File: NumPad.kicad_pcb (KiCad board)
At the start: 2 copper layers, 60.7 x 98.9 mm, 112 parts, among them J1 Micro_SD_Card_Det, J2 OLED1, J3 OLED2, J4 Conn_01x05_Female, SW1 SW_SPST, SW10 SW_SPST, SW11 SW_SPST, SW12 SW_SPST, SW13 SW_SPST, SW14 SW_SPST, SW15 SW_SPST, SW16 SW_SPST, SW17 SW_SPST, SW18 SW_SPST, SW19 SW_SPST, SW2 SW_SPST, SW20 SW_SPST, SW21 SW_SPST, SW22 SW_SPST, SW23 SW_SPST, SW24 SW_SPST, SW25 SW_BUTTONRESET, SW26 SW_BUTTON2, SW27 SW_BUTTON1, SW28 SW_BOOT0, SW29 Rotary_Encoder_Switch, SW3 SW_SPST, SW4 SW_SPST, SW5 SW_SPST, SW6 SW_SPST, SW7 SW_SPST, SW8 SW_SPST, SW9 SW_SPST, U1 LM117_TO3, U2 STM32F072C8Tx, U3 74AHCT1G08

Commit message: PCB Update
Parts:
- C1, C12, C13, C2, C3, C4, C5, C6, C7, C9, D10, D11, D12, D13, D14, D15, D16, D17, D18, D19, D2, D20, D21, D22, D23, D24, D25, D3, D4, D5, D6, D7, D8, D9, R1, R10, R2, R3, R6, R7, U1, U3: moved to B.Cu
- moved R10 159.1 mm to (71.5, 55.2)
- moved C6 148.5 mm to (27.7, 166.0)
- moved R9 141.5 mm to (94.6, 57.1)
- moved R8 136.8 mm to (95.3, 62.7)
- moved C3 135.1 mm to (46.7, 166.0)
- moved R5 126.2 mm to (119.4, 174.6)
- moved J4 123.0 mm to (104.8, 178.6), turned to 90 degrees
- moved U3 122.1 mm to (103.8, 69.9), turned to 270 degrees
- moved R7 121.4 mm to (103.8, 75.2)
- moved C2 109.0 mm to (116.8, 83.4)
- moved C1 108.7 mm to (116.8, 80.3)
- moved R4 102.1 mm to (127.7, 174.9)
- moved R1 98.8 mm to (130.8, 73.4)
- moved R3 96.9 mm to (151.3, 78.8)
- moved R2 93.3 mm to (124.1, 72.6)
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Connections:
- C1 pad 2: +5V -> GND
- C10 pad 2: +5V -> GND
- C11 pad 2: +5V -> GND
- C12 pad 2: +5V -> GND
- C13 pad 2: +5V -> GND
- C14 pad 2: +5V -> GND
- C2 pad 2: +5V -> GND
- C3 pad 2: +5V -> GND
- C4 pad 2: +5V -> GND
- C5 pad 2: +5V -> GND
- C6 pad 2: +5V -> GND
- C7 pad 2: +5V -> GND
- C8 pad 2: +5V -> GND
- C9 pad 2: +5V -> GND
- D1 pad 1: +5V -> GND
- D26 pad 2: Net-(D32-Pad2) -> Net-(D26-Pad2)
- D26 pad 3: +5V -> GND
- D26 pad 4: Net-(D26-Pad2) -> Net-(D26-Pad4)
- D27 pad 2: Net-(D32-Pad2) -> Net-(D27-Pad2)
- D27 pad 3: +5V -> GND
- D27 pad 4: Net-(D26-Pad2) -> Net-(D27-Pad4)
- D28 pad 2: Net-(D32-Pad2) -> Net-(D28-Pad2)
- D28 pad 3: +5V -> GND
- D28 pad 4: Net-(D26-Pad2) -> Net-(D28-Pad4)
- D29 pad 2: Net-(D32-Pad2) -> Net-(D29-Pad2)
- D29 pad 3: +5V -> GND
- D29 pad 4: Net-(D26-Pad2) -> Net-(D29-Pad4)
- D30 pad 2: Net-(D32-Pad2) -> Net-(D30-Pad2)
- D30 pad 3: +5V -> GND
- D30 pad 4: Net-(D26-Pad2) -> Net-(D30-Pad4)
- D31 pad 2: Net-(D32-Pad2) -> Net-(D31-Pad2)
- D31 pad 3: +5V -> GND
- D31 pad 4: Net-(D26-Pad2) -> Net-(D31-Pad4)
- D32 pad 3: +5V -> GND
- D33 pad 2: Net-(D32-Pad2) -> Net-(D33-Pad2)
- D33 pad 3: +5V -> GND
- D33 pad 4: Net-(D26-Pad2) -> Net-(D27-Pad2)
- D34 pad 2: Net-(D32-Pad2) -> Net-(D34-Pad2)
- D34 pad 3: +5V -> GND
- D34 pad 4: Net-(D26-Pad2) -> Net-(D28-Pad2)
- D35 pad 2: Net-(D32-Pad2) -> Net-(D35-Pad2)
- D35 pad 3: +5V -> GND
- D35 pad 4: Net-(D26-Pad2) -> Net-(D29-Pad2)
- D36 pad 2: Net-(D32-Pad2) -> Net-(D36-Pad2)
- D36 pad 3: +5V -> GND
- D36 pad 4: Net-(D26-Pad2) -> Net-(D30-Pad2)
- D37 pad 2: Net-(D32-Pad2) -> Net-(D37-Pad2)
- D37 pad 3: +5V -> GND
- D37 pad 4: Net-(D26-Pad2) -> Net-(D31-Pad2)
- D38 pad 2: Net-(D32-Pad2) -> Net-(D38-Pad2)
- D38 pad 3: +5V -> GND
- D38 pad 4: Net-(D26-Pad2) -> Net-(D32-Pad2)
- D39 pad 2: Net-(D32-Pad2) -> Net-(D39-Pad2)
- D39 pad 3: +5V -> GND
- D39 pad 4: Net-(D26-Pad2) -> Net-(D33-Pad2)
- D40 pad 2: Net-(D32-Pad2) -> Net-(D40-Pad2)
- D40 pad 3: +5V -> GND
- D40 pad 4: Net-(D26-Pad2) -> Net-(D34-Pad2)
- D41 pad 2: Net-(D32-Pad2) -> Net-(D41-Pad2)
- D41 pad 3: +5V -> GND
- D41 pad 4: Net-(D26-Pad2) -> Net-(D35-Pad2)
- D42 pad 2: Net-(D32-Pad2) -> Net-(D42-Pad2)
- D42 pad 3: +5V -> GND
- D42 pad 4: Net-(D26-Pad2) -> Net-(D36-Pad2)
- D43 pad 2: Net-(D32-Pad2) -> Net-(D43-Pad2)
- D43 pad 3: +5V -> GND
- D43 pad 4: Net-(D26-Pad2) -> Net-(D37-Pad2)
- D44 pad 2: Net-(D32-Pad2) -> Net-(D27-Pad4)
- D44 pad 3: +5V -> GND
- D44 pad 4: Net-(D26-Pad2) -> Net-(D38-Pad2)
- D45 pad 2: Net-(D32-Pad2) -> Net-(D28-Pad4)
- D45 pad 3: +5V -> GND
- D45 pad 4: Net-(D26-Pad2) -> Net-(D39-Pad2)
- D46 pad 2: Net-(D32-Pad2) -> Net-(D29-Pad4)
- D46 pad 3: +5V -> GND
- D46 pad 4: Net-(D26-Pad2) -> Net-(D40-Pad2)
- D47 pad 2: Net-(D32-Pad2) -> Net-(D30-Pad4)
- D47 pad 3: +5V -> GND
- D47 pad 4: Net-(D26-Pad2) -> Net-(D41-Pad2)
- D48 pad 2: Net-(D32-Pad2) -> Net-(D31-Pad4)
- D48 pad 3: +5V -> GND
- D48 pad 4: Net-(D26-Pad2) -> Net-(D42-Pad2)
- D49 pad 2: Net-(D32-Pad2) -> Net-(D49-Pad2)
- D49 pad 3: +5V -> GND
- D49 pad 4: Net-(D26-Pad2) -> Net-(D43-Pad2)
- J1 pad 11: +5V -> GND
- J1 pad 6: +5V -> GND
- J2 pad 3: +5V -> GND
- J3 pad 3: +5V -> GND
- J4 pad 4: +5V -> GND
- R1 pad 1: +5V -> GND
- R2 pad 1: +5V -> GND
- R6 pad 2: +5V -> GND
- R7 pad 1: +5V -> GND
- RV1 pad 1: +5V -> GND
- SW25 pad 1: +5V -> GND
- SW26 pad 2: +5V -> GND
- SW27 pad 2: +5V -> GND
- SW29 pad C: +5V -> GND
- SW29 pad S2: +5V -> GND
- U1 pad 1: +5V -> GND
- U2 pad 1: +5V -> GND
- U2 pad 23: +5V -> GND
- U2 pad 35: +5V -> GND
- U2 pad 47: +5V -> GND
- U2 pad 8: +5V -> GND
- U3 pad 3: +5V -> GND
- USB1 pad 1: +5V -> GND
- USB1 pad 12: +5V -> GND
- USB1 pad 13: +5V -> GND

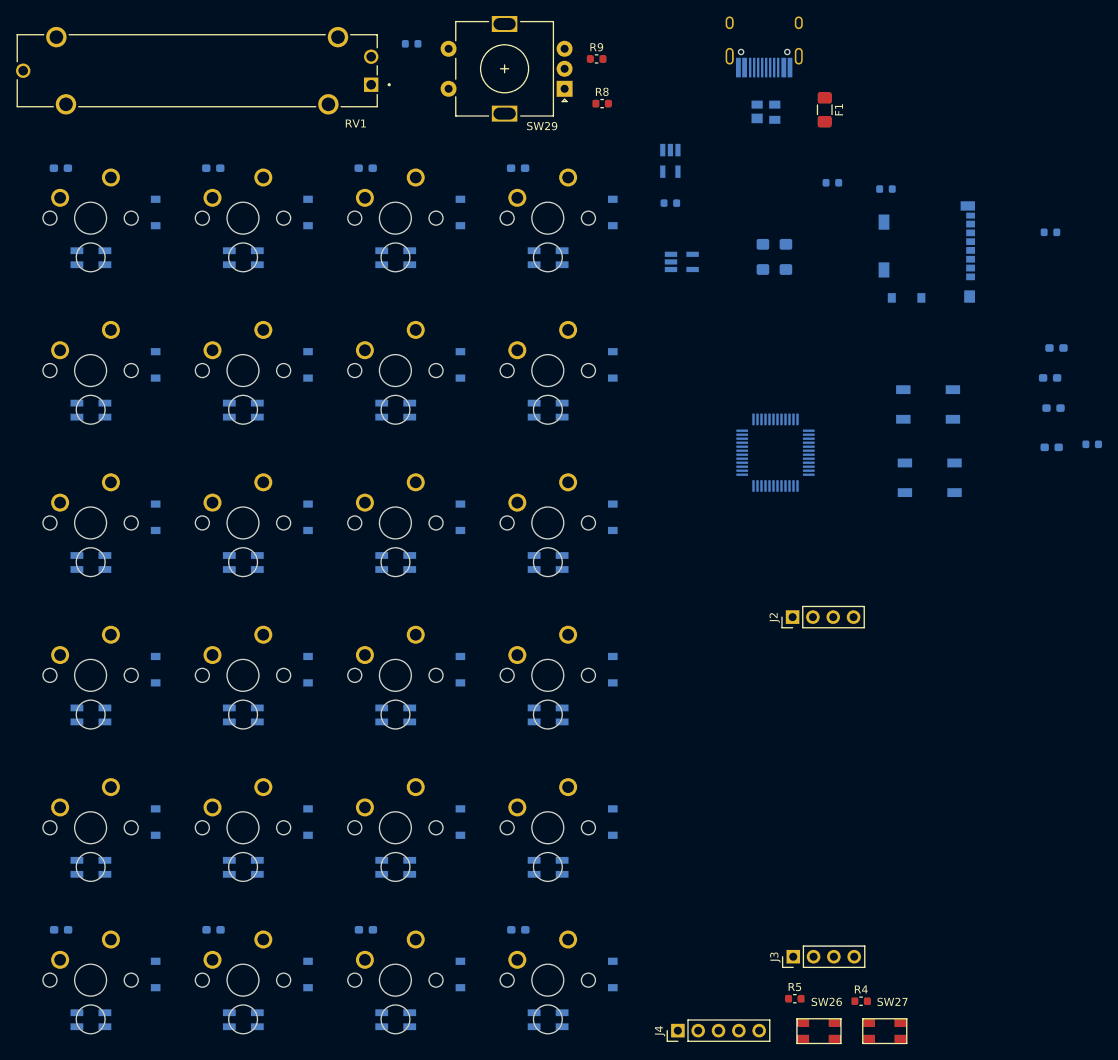
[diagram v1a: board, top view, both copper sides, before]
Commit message: Add footprints libs
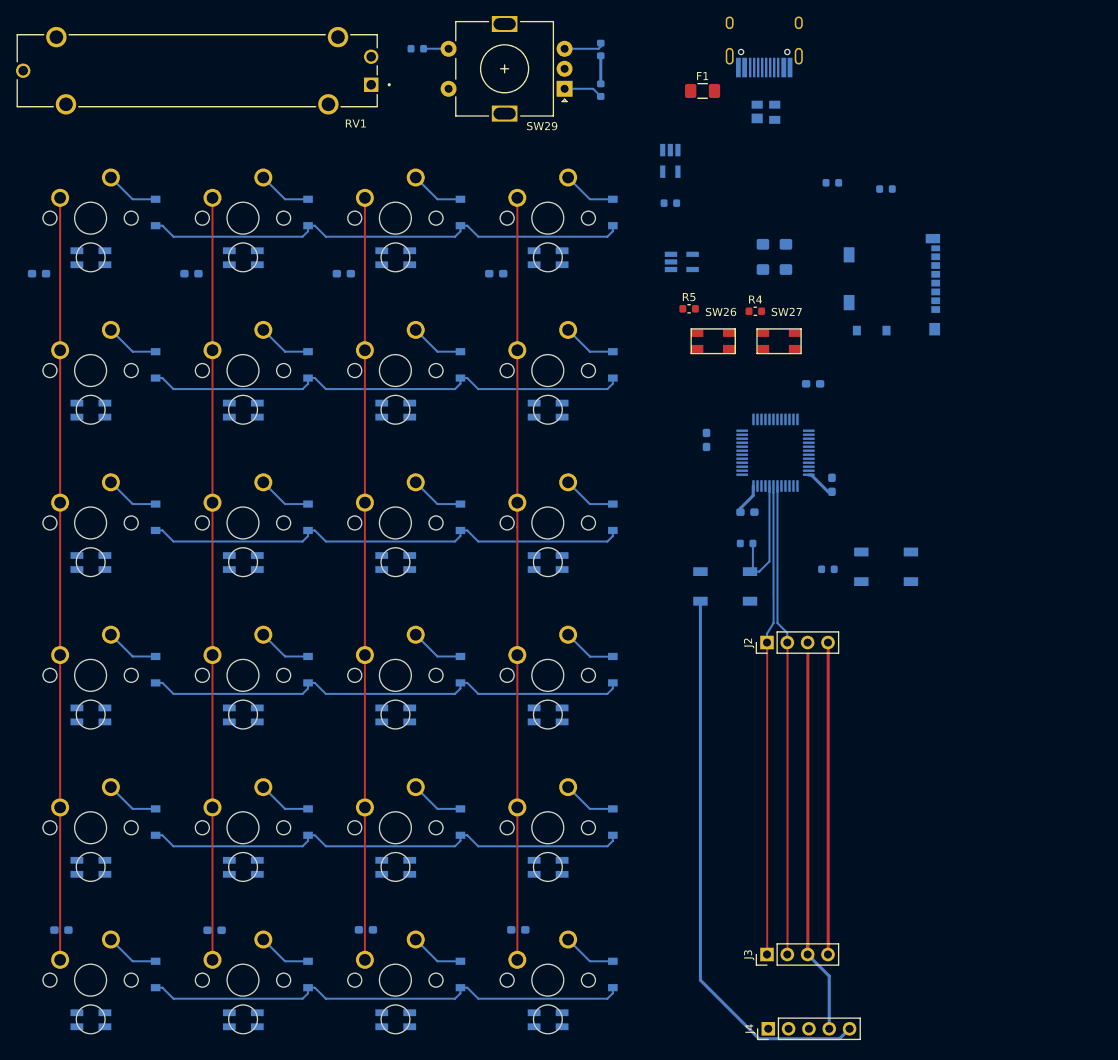
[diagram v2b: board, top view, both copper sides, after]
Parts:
- R8, R9: moved to B.Cu
- moved C12 140.1 mm to (27.7, 166.0), turned to 180 degrees
- moved C7 120.8 mm to (46.9, 166.0)
- moved C6 100.4 mm to (113.5, 113.8)
- moved SW26 87.2 mm to (110.2, 92.4)
- moved SW27 87.2 mm to (118.4, 92.4)
- moved R4 87.2 mm to (114.5, 88.7)
- moved R5 87.2 mm to (106.2, 88.4)
- moved C3 86.9 mm to (108.3, 104.8), turned to 270 degrees
- moved R3 50.5 mm to (123.5, 120.9)
- moved R6 44.9 mm to (113.4, 117.7), turned to 180 degrees
- moved SW28 34.1 mm to (110.7, 123.1)
- moved C4 30.7 mm to (121.7, 97.7), turned to 180 degrees
- moved C5 30.4 mm to (124.0, 110.4), turned to 90 degrees
- moved F1 15.5 mm to (107.9, 61.1), turned to 0 degrees
- moved C10 13.5 mm to (44.0, 84.0), turned to 180 degrees
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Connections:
- C10 pad 1: +3V3 -> +5V
- C11 pad 1: +3V3 -> +5V
- C12 pad 1: +3V3 -> +5V
- C13 pad 1: +3V3 -> +5V
- C14 pad 1: +3V3 -> +5V
- C7 pad 1: +3V3 -> +5V
- C8 pad 1: +3V3 -> +5V
- C9 pad 1: +3V3 -> +5V
- U2 pad 25: col3 -> POT_SLIDER
- U2 pad 26: row0 -> Net-(U2-Pad26)
- U2 pad 27: row1 -> Net-(U2-Pad27)
- U2 pad 28: row2 -> Net-(U2-Pad28)
- U2 pad 29: row3 -> Net-(U2-Pad29)
- U2 pad 3: Net-(U2-Pad3) -> col3
- U2 pad 4: Net-(U2-Pad4) -> row0
- U2 pad 40: POT_SLIDER -> Net-(U2-Pad40)
- U2 pad 45: Net-(U2-Pad45) -> row3
- U2 pad 5: Net-(U2-Pad5) -> row1
- U2 pad 6: Net-(U2-Pad6) -> row2
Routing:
- net col3: track 0.00 -> 95.2 mm
- net col2: track 0.00 -> 95.2 mm
- net col1: track 0.00 -> 95.2 mm
- net col0: track 0.00 -> 95.2 mm
- net +3V3: track 0.00 -> 80.8 mm
- net row4: track 0.00 -> 61.8 mm
- net row5: track 0.00 -> 61.8 mm
- net row2: track 0.00 -> 61.8 mm
- net row1: track 0.00 -> 61.8 mm
- net row0: track 0.00 -> 61.8 mm
- net row3: track 0.00 -> 61.8 mm
- net SCK: track 0.00 -> 59.1 mm
- net SDA: track 0.00 -> 58.0 mm
- net GND: track 0.00 -> 49.4 mm
- net +5V: track 0.00 -> 39.0 mm
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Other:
- net class Default: via_dia 0.8 -> 0.6
- net class power added: clearance 0.2, trace_width 0.38, via_dia 0.6, via_drill 0.4

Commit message: Update PCB
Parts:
- D26, D27, D28, D29, D30, D31, D32, D33, D34, D35, D36, D37, D38, D39, D40, D41, D42, D43, D44, D45, D46, D47, D48, D49: footprint LED_SMD:LED_SK6812MINI_PLCC4_3.5x3.5mm_P1.75mm -> keyboard_parts:YS-SK6812MINI-E
- moved C4 1.19 mm to (121.7, 96.5)
- turned D26 to 0 degrees
- turned D27 to 0 degrees
- turned D28 to 0 degrees
- turned D29 to 0 degrees
- turned D30 to 0 degrees
- turned D31 to 0 degrees
- turned D32 to 0 degrees
- turned D33 to 0 degrees
- turned D34 to 0 degrees
- turned D35 to 0 degrees
- turned D36 to 0 degrees
- turned D37 to 0 degrees
- turned D38 to 0 degrees
- turned D39 to 0 degrees
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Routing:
- net +5V: track 39.0 -> 112.1 mm, vias 0 -> 1
- net SPI_MISO: track 0.00 -> 35.8 mm, vias 0 -> 3
- net SPI_SCK: track 0.00 -> 34.9 mm, vias 0 -> 2
- net SPI_MOSI: track 0.00 -> 31.8 mm
- net SD_CS: track 0.00 -> 30.4 mm
- net +3V3: track 80.8 -> 103.6 mm
- net Detec: track 0.00 -> 19.8 mm
- net Net-(D31-Pad2): track 0.00 -> 14.7 mm
- net Net-(D30-Pad2): track 0.00 -> 14.7 mm
- net Net-(D29-Pad2): track 0.00 -> 14.7 mm
- net Net-(D28-Pad2): track 0.00 -> 14.7 mm
- net Net-(D27-Pad2): track 0.00 -> 14.7 mm
- net Net-(D26-Pad2): track 0.00 -> 14.7 mm
- net Net-(D43-Pad2): track 0.00 -> 14.7 mm
- net Net-(D42-Pad2): track 0.00 -> 14.7 mm
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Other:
- outline, holes or cut-outs redrawn

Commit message: update PCB
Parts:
- D1: footprint Package_TO_SOT_SMD:SOT-143 -> random-keyboard-parts:SOT143B
- F1: moved to B.Cu
- R8, R9: moved to F.Cu
- moved SW25 35.2 mm to (100.5, 102.8), turned to 90 degrees
- moved U1 27.5 mm to (129.1, 68.8), turned to 90 degrees
- moved J2 26.6 mm to (116.0, 103.4)
- moved J3 26.3 mm to (115.9, 142.8)
- moved R3 23.9 mm to (103.1, 108.5), turned to 180 degrees
- moved R1 21.7 mm to (111.4, 63.5)
- moved C4 16.1 mm to (123.4, 112.6), turned to 90 degrees
- moved C1 14.6 mm to (130.5, 75.1), turned to 270 degrees
- moved C5 11.9 mm to (124.0, 122.3)
- moved SW28 11.9 mm to (110.7, 135.0)
- moved U2 11.9 mm to (117.0, 118.3)
- moved C6 11.9 mm to (113.5, 125.7)
- moved R2 11.7 mm to (118.8, 62.2), turned to 90 degrees
- moved C3 11.3 mm to (108.3, 116.1)
- moved R6 11.2 mm to (114.2, 128.8), turned to 90 degrees
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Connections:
- R5 pad 2: Net-(R5-Pad2) -> BUT2
- SW26 pad 1: Net-(R5-Pad2) -> BUT2
- U2 pad 12: row4 -> col3
- U2 pad 13: Net-(R5-Pad2) -> row0
- U2 pad 25: POT_SLIDER -> BUT1
- U2 pad 26: Net-(U2-Pad26) -> BUT2
- U2 pad 27: Net-(U2-Pad27) -> POT_SLIDER
- U2 pad 28: Net-(U2-Pad28) -> ENC_SWITCH
- U2 pad 3: col3 -> row4
- U2 pad 38: BUT1 -> Net-(U2-Pad38)
- U2 pad 39: ENC_SWITCH -> Net-(U2-Pad39)
- U2 pad 4: row0 -> row3
- U2 pad 45: row3 -> Net-(U2-Pad45)
- U2 pad 5: row1 -> row2
- U2 pad 6: row2 -> row1
- U3 pad 5: VCC -> +5V
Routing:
- net +5V: track 112.1 -> 737.3 mm, vias 1 -> 7
- net GND: track 56.1 -> 528.2 mm, vias 0 -> 15
- net +3V3: track 103.6 -> 337.7 mm, vias 0 -> 9
- net col1: track 95.2 -> 238.1 mm, vias 0 -> 1
- net POT_SLIDER: track 0.00 -> 110.3 mm, vias 0 -> 1
- net col0: track 95.2 -> 192.2 mm, vias 0 -> 3
- net ENC_SWITCH: track 3.13 -> 98.9 mm, vias 0 -> 2
- net Net-(D31-Pad4): track 0.00 -> 92.8 mm
- net Net-(D26-Pad4): track 0.00 -> 91.5 mm
- net Net-(D27-Pad4): track 0.00 -> 90.5 mm
- net Net-(D30-Pad4): track 0.00 -> 90.4 mm
- net Net-(D29-Pad4): track 0.00 -> 90.0 mm
- net Net-(D28-Pad4): track 0.00 -> 90.0 mm
- net USB_DN: track 0.00 -> 76.7 mm, vias 0 -> 2
- net USB_DP: track 0.00 -> 76.0 mm, vias 0 -> 2
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- added copper zone on B.Cu, net GND
- added copper zone on F.Cu, net GND
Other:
- board size 60.7 x 98.9 mm -> 120.1 x 132.9 mm

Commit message: Update PCB
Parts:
- moved R10 1.43 mm to (73.2, 56.9), turned to 270 degrees
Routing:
- net +3V3: track 337.7 -> 335.9 mm
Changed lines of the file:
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@@
     (thickness 1.6)
     (drawings 108)
-    (tracks 1128)
+    (tracks 1127)
     (zones 0)
     (modules 112)
@@
   )
   (module Resistor_SMD:R_0603_1608Metric (layer B.Cu)
-    (at 72.2 55.85 180)
+    (at 73.2 56.875 270)
     (descr "Resistor SMD 0603 (1608 Metric), square (rectangular) end terminal, IPC_7351 nominal, (Body size source: http://www.tortai-tech.com/upload/download/2011102023233369053.pdf), generated with kicad-footprint-generator")
     (tags resistor)
     (attr smd)
-    (fp_text reference R10 (at 0 1.43) (layer B.SilkS)
+    (fp_text reference R10 (at 0 1.43 90) (layer B.SilkS)
       (effects (font (size 1 1) (thickness 0.15)) (justify mirror))
     )
-    (fp_text value 10K (at 0 -1.43) (layer B.Fab)
+    (fp_text value 10K (at 0 -1.43 90) (layer B.Fab)
       (effects (font (size 1 1) (thickness 0.15)) (justify mirror))
     )
-    (fp_text user %R (at 0 0) (layer B.Fab)
+    (fp_text user %R (at 0 0 90) (layer B.Fab)
       (effects (font (size 0.4 0.4) (thickness 0.06)) (justify mirror))
     )
@@
     (fp_line (start -0.8 0.4) (end 0.8 0.4) (layer B.Fab) (width 0.1))
     (fp_line (start -0.8 -0.4) (end -0.8 0.4) (layer B.Fab) (width 0.1))
-    (pad 2 smd roundrect (at 0.7875 0 180) (size 0.875 0.95) (layers B.Cu B.Paste B.Mask) (roundrect_rratio 0.25)
+    (pad 2 smd roundrect (at 0.7875 0 270) (size 0.875 0.95) (layers B.Cu B.Paste B.Mask) (roundrect_rratio 0.25)
       (net 2 +3V3))
-    (pad 1 smd roundrect (at -0.7875 0 180) (size 0.875 0.95) (layers B.Cu B.Paste B.Mask) (roundrect_rratio 0.25)
+    (pad 1 smd roundrect (at -0.7875 0 270) (size 0.875 0.95) (layers B.Cu B.Paste B.Mask) (roundrect_rratio 0.25)
       (net 65 ENC_SWITCH))
     (model ${KISYS3DMOD}/Resistor_SMD.3dshapes/R_0603_1608Metric.wrl
@@
   (segment (start 113.225 87.775) (end 112.6 88.4) (width 0.38) (layer F.Cu) (net 2))
   (segment (start 113.225 87.3) (end 113.225 87.775) (width 0.38) (layer F.Cu) (net 2))
-  (segment (start 24.207793 58.6) (end 22.935001 58.6) (width 0.38) (layer B.Cu) (net 2))
-  (segment (start 69.1375 58.6) (end 24.207793 58.6) (width 0.38) (layer B.Cu) (net 2))
-  (segment (start 71.4125 56.325) (end 69.1375 58.6) (width 0.38) (layer B.Cu) (net 2))
-  (segment (start 71.4125 55.85) (end 71.4125 56.325) (width 0.38) (layer B.Cu) (net 2))
   (segment (start 95.1325 60.2425) (end 95.1325 56.7275) (width 0.38) (layer F.Cu) (net 2))
   (via (at 93.925 60.225) (size 0.6) (drill 0.4) (layers F.Cu B.Cu) (net 2))
@@
   (segment (start 112.6 97.525) (end 112.55 97.575) (width 0.38) (layer F.Cu) (net 2))
   (segment (start 112.6 96.05) (end 112.6 97.525) (width 0.38) (layer F.Cu) (net 2))
-  (segment (start 91.899999 62.250001) (end 93.925 60.225) (width 0.38) (layer B.Cu) (net 2))
-  (segment (start 71.651582 55.85) (end 74.075 58.575) (width 0.38) (layer B.Cu) (net 2))
-  (segment (start 71.4125 55.85) (end 71.651582 55.85) (width 0.38) (layer B.Cu) (net 2))
-  (segment (start 74.075 58.575) (end 85.25 58.575) (width 0.38) (layer B.Cu) (net 2))
-  (segment (start 85.25 58.575) (end 89.297999 62.250001) (width 0.38) (layer B.Cu) (net 2))
-  (segment (start 89.297999 62.250001) (end 91.899999 62.250001) (width 0.38) (layer B.Cu) (net 2))
   (segment (start 113.545 117.03) (end 112.8075 117.03) (width 0.2) (layer B.Cu) (net 2))
   (segment (start 113.575346 117.03) (end 113.545 117.03) (width 0.2) (layer B.Cu) (net 2))
@@
   (segment (start 108.675 69.795) (end 105.825 66.945) (width 0.38) (layer F.Cu) (net 2))
   (segment (start 108.675 71) (end 108.675 69.795) (width 0.38) (layer F.Cu) (net 2))
+  (segment (start 72.7 58.6) (end 73.2 58.1) (width 0.38) (layer B.Cu) (net 2))
+  (segment (start 22.935001 58.6) (end 72.7 58.6) (width 0.38) (layer B.Cu) (net 2))
+  (segment (start 91.899999 62.250001) (end 93.925 60.225) (width 0.38) (layer B.Cu) (net 2))
+  (segment (start 73.675 58.575) (end 85.25 58.575) (width 0.38) (layer B.Cu) (net 2))
+  (segment (start 73.2 57.6625) (end 73.2 58.1) (width 0.38) (layer B.Cu) (net 2))
+  (segment (start 85.25 58.575) (end 89.297999 62.250001) (width 0.38) (layer B.Cu) (net 2))
+  (segment (start 73.2 58.1) (end 73.675 58.575) (width 0.38) (layer B.Cu) (net 2))
+  (segment (start 89.297999 62.250001) (end 91.899999 62.250001) (width 0.38) (layer B.Cu) (net 2))
   (segment (start 116.31 59.63) (end 116.31 58.205) (width 0.2) (layer B.Cu) (net 3))
   (segment (start 116.209999 59.730001) (end 116.31 59.63) (width 0.2) (layer B.Cu) (net 3))
@@
   (segment (start 93.74 55.86) (end 94.4475 55.1525) (width 0.25) (layer F.Cu) (net 64))
   (segment (start 76.1 55.85) (end 76.11 55.86) (width 0.25) (layer B.Cu) (net 65))
-  (segment (start 72.9875 55.85) (end 76.1 55.85) (width 0.25) (layer B.Cu) (net 65))
   (segment (start 77.435001 54.534999) (end 91.209999 54.534999) (width 0.25) (layer B.Cu) (net 65))
   (segment (start 76.11 55.86) (end 77.435001 54.534999) (width 0.25) (layer B.Cu) (net 65))
@@
   (segment (start 123.480004 117.03) (end 121.1325 117.03) (width 0.25) (layer B.Cu) (net 65))
   (segment (start 123.525004 117.075) (end 123.480004 117.03) (width 0.25) (layer B.Cu) (net 65))
+  (segment (start 75.8825 56.0875) (end 76.11 55.86) (width 0.25) (layer B.Cu) (net 65))
+  (segment (start 73.2 56.0875) (end 75.8825 56.0875) (width 0.25) (layer B.Cu) (net 65))
   (segment (start 93.295403 51.434999) (end 98.875 57.014596) (width 0.25) (layer F.Cu) (net 66))
   (segment (start 66.435001 56.85) (end 71.850002 51.434999) (width 0.25) (layer F.Cu) (net 66))
